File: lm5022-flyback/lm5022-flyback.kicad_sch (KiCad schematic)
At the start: 55 parts, among them Q1 EPC2302, SW1 SW_Nidec_CAS-120A1, T1 Arthur, U1 LM5022MM, U2 TLVH431BQDCKT, U3 LTV-817-C

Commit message: euler work
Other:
- note added: "TODO: Resize D1 to be rated for 400V + reflected primary voltage (roughly 2x rating)"
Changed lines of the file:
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@@
+		)
+	)
+	(text "TODO: Resize D1 to be rated for 400V + reflected primary voltage (roughly 2x rating)"
+		(exclude_from_sim no)
+		(at 189.992 32.258 0)
+		(effects
+			(font
+				(size 1.27 1.27)
+			)
 		)
 	)

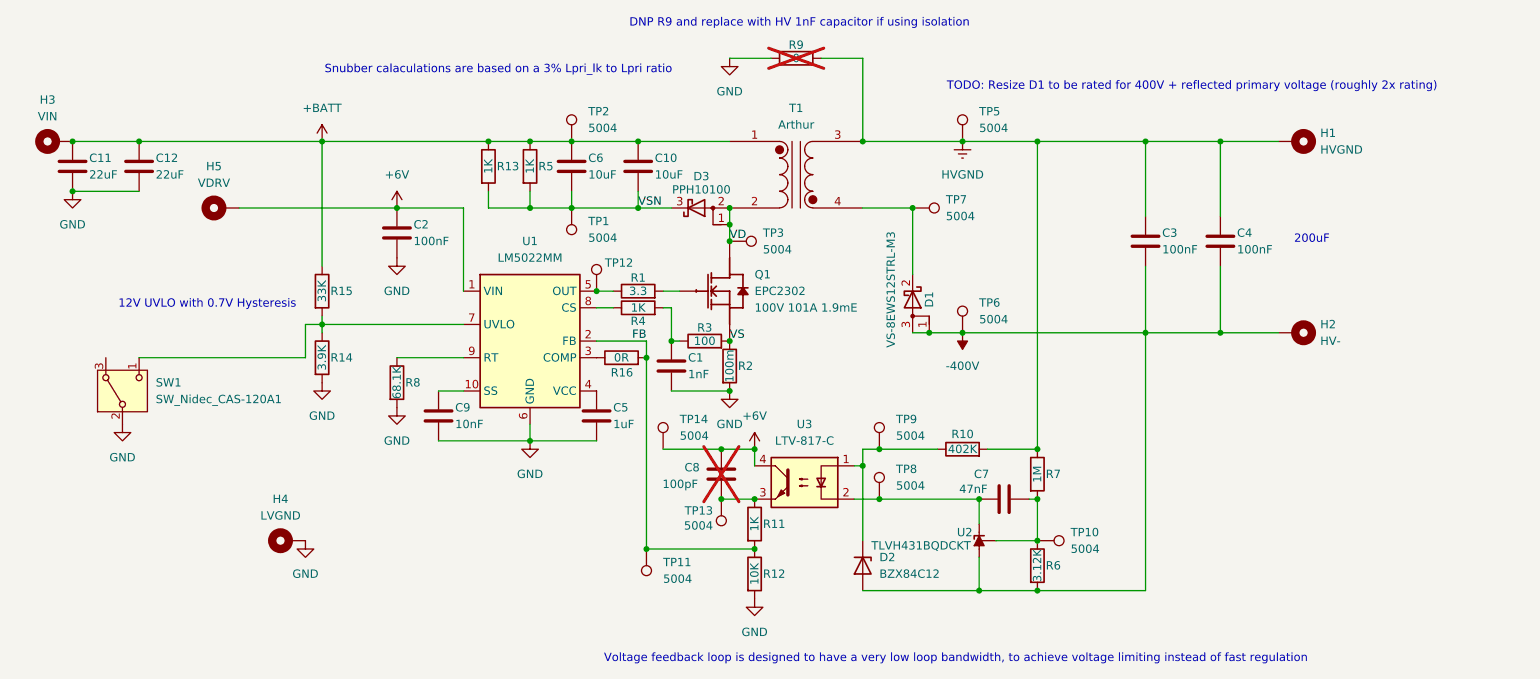
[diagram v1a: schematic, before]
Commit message: rev 2 of 400V converter
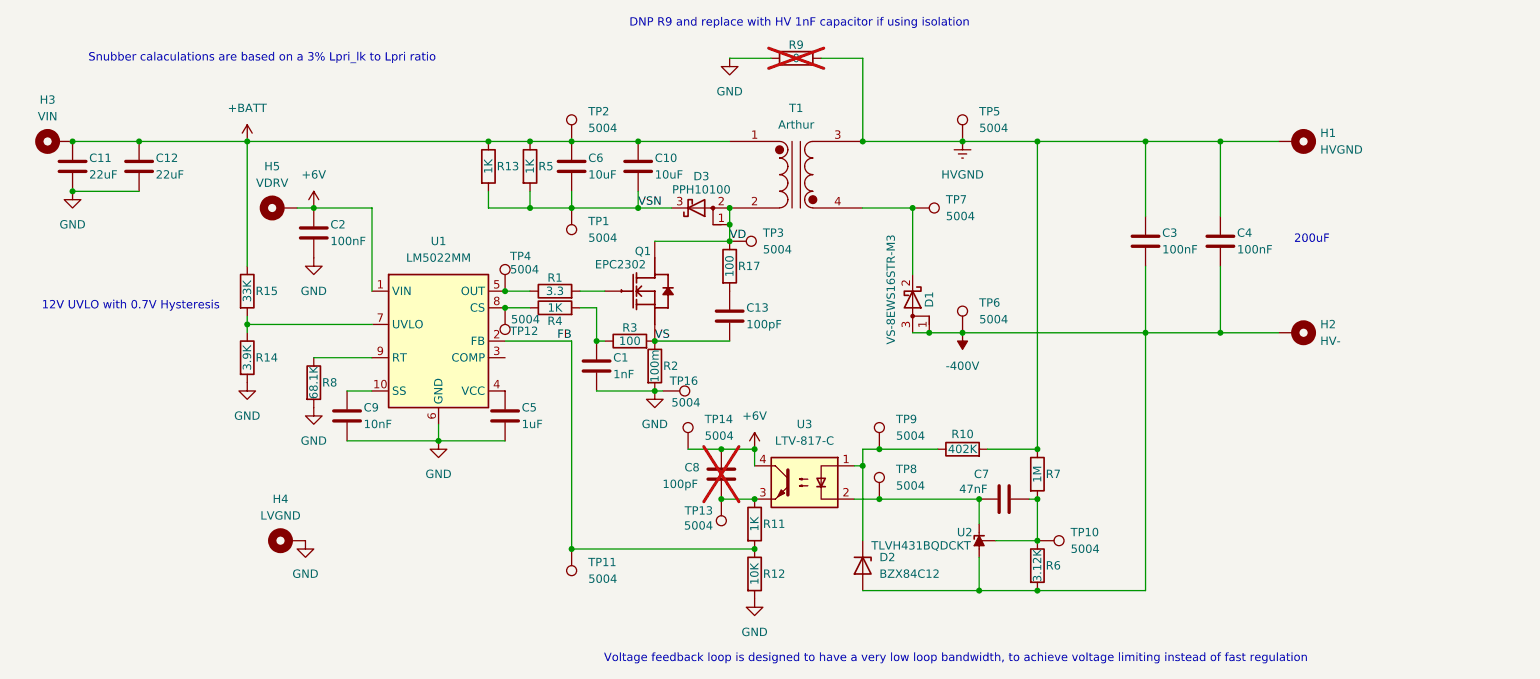
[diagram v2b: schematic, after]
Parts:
- removed R16: 0R, Resistor_SMD:R_0402_1005Metric, symbol Device:R
- removed SW1: SW_Nidec_CAS-120A1, Button_Switch_SMD:Nidec_Copal_CAS-120A, symbol Switch:SW_Nidec_CAS-120A1
- added C13: 100pF, Capacitor_SMD:C_0603_1608Metric, symbol Device:C
- added R17: 100, Resistor_SMD:R_0603_1608Metric, symbol Device:R
- added TP16, TP4: 5004, TestPoint:TestPoint_Keystone_5000-5004_Miniature, symbol Connector:TestPoint
- D1: value VS-8EWS12STRL-M3 -> VS-8EWS16STR-M3
- TP12: value ~ -> 5004; footprint TestPoint:TestPoint_Pad_D1.0mm -> TestPoint:TestPoint_Keystone_5000-5004_Miniature
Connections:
- net GND: now also TP16.1
- net VD: now also R17.1
- net VS: now also C13.2
- net at R4.1, U1.8 (CS): now also TP12.1
- net at R1.1, U1.5 (OUT): now also TP4.1; no longer TP12.1
- new net: C13.1, R17.2
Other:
- note removed: "TODO: Resize D1 to be rated for 400V + reflected primary voltage (roughly 2x rating)"
- moved on the sheet: C1, C2, C5, C9, H5, Q1, R1, R14, R15, R2, R3, R4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
